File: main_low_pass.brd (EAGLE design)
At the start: 45.4 x 25.6 mm, 16 parts, among them IC1 74HC14D, X1 14867

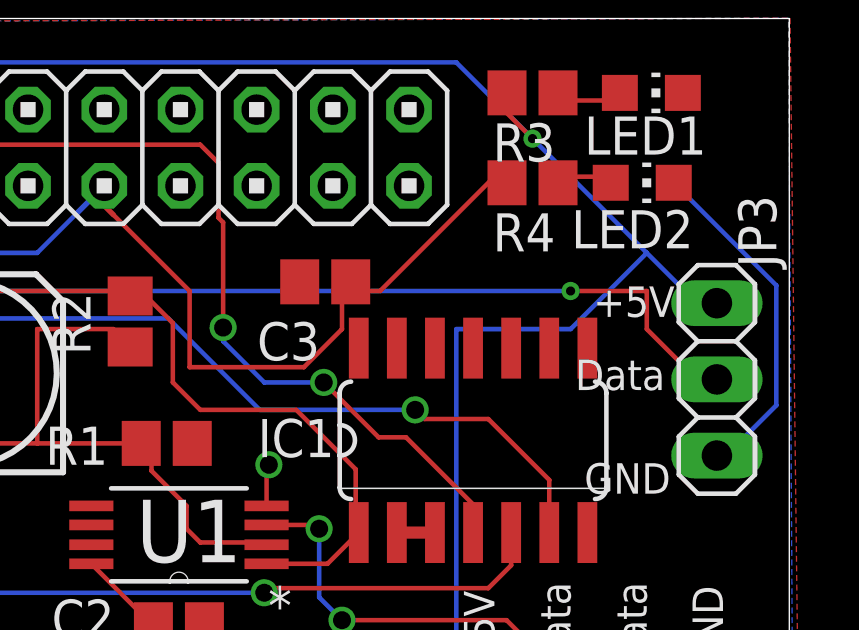
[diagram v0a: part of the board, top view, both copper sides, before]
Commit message: First set of fixes: Missed some connections to IC1
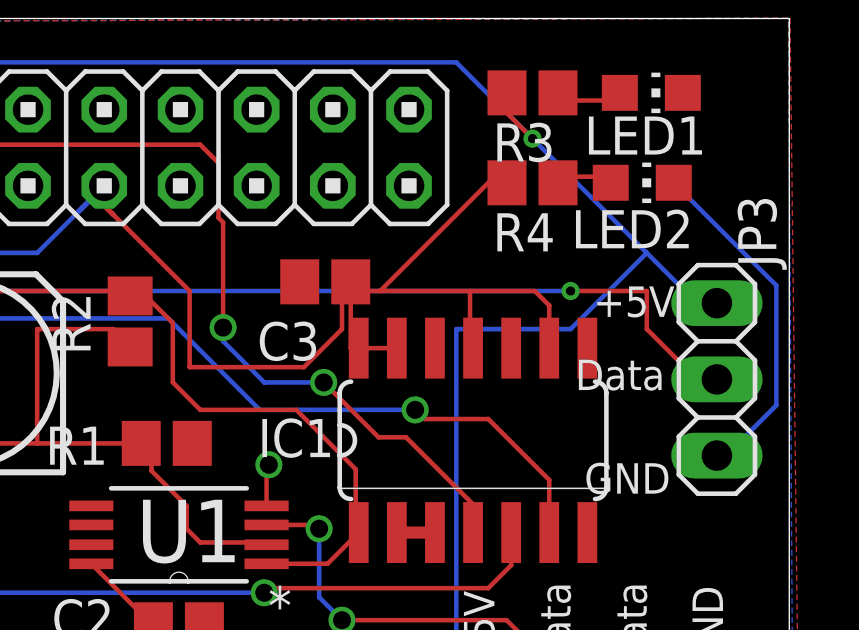
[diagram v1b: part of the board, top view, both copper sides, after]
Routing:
- net VCC: track 44.9 -> 57.9 mm
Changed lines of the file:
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@@
 <wire x1="22.86" y1="17.78" x2="22.5552" y2="18.0848" width="0.1778" layer="1"/>
 <wire x1="22.5552" y1="18.0848" x2="22.5552" y2="18.7452" width="0.1778" layer="1"/>
-<wire x1="34.8488" y1="13.335" x2="37.3888" y2="13.335" width="0" layer="19" extent="1-1"/>
-<wire x1="32.3088" y1="13.335" x2="34.8488" y2="13.335" width="0" layer="19" extent="1-1"/>
-<wire x1="31.0388" y1="13.335" x2="32.3088" y2="13.335" width="0" layer="19" extent="1-1"/>
-<wire x1="30.48" y1="13.97" x2="31.0388" y2="13.335" width="0" layer="19" extent="1-1"/>
+<wire x1="30.7712" y1="13.335" x2="30.7712" y2="15.5448" width="0.1524" layer="1"/>
+<wire x1="37.3888" y1="13.335" x2="37.3888" y2="14.7574" width="0.1524" layer="1"/>
+<wire x1="37.3888" y1="14.7574" x2="36.9062" y2="15.24" width="0.1524" layer="1"/>
+<wire x1="36.9062" y1="15.24" x2="34.7472" y2="15.24" width="0.1524" layer="1"/>
+<wire x1="34.7472" y1="15.24" x2="31.75" y2="15.24" width="0.1524" layer="1"/>
+<wire x1="34.8488" y1="13.335" x2="34.7472" y2="13.4366" width="0.1524" layer="1"/>
+<wire x1="34.7472" y1="13.4366" x2="34.7472" y2="15.24" width="0.1524" layer="1"/>
+<wire x1="32.3088" y1="13.335" x2="31.0388" y2="13.335" width="0.1524" layer="1"/>
+<wire x1="30.7712" y1="13.335" x2="31.0388" y2="13.335" width="0.1524" layer="1"/>
 </signal>
 <signal name="N$3">

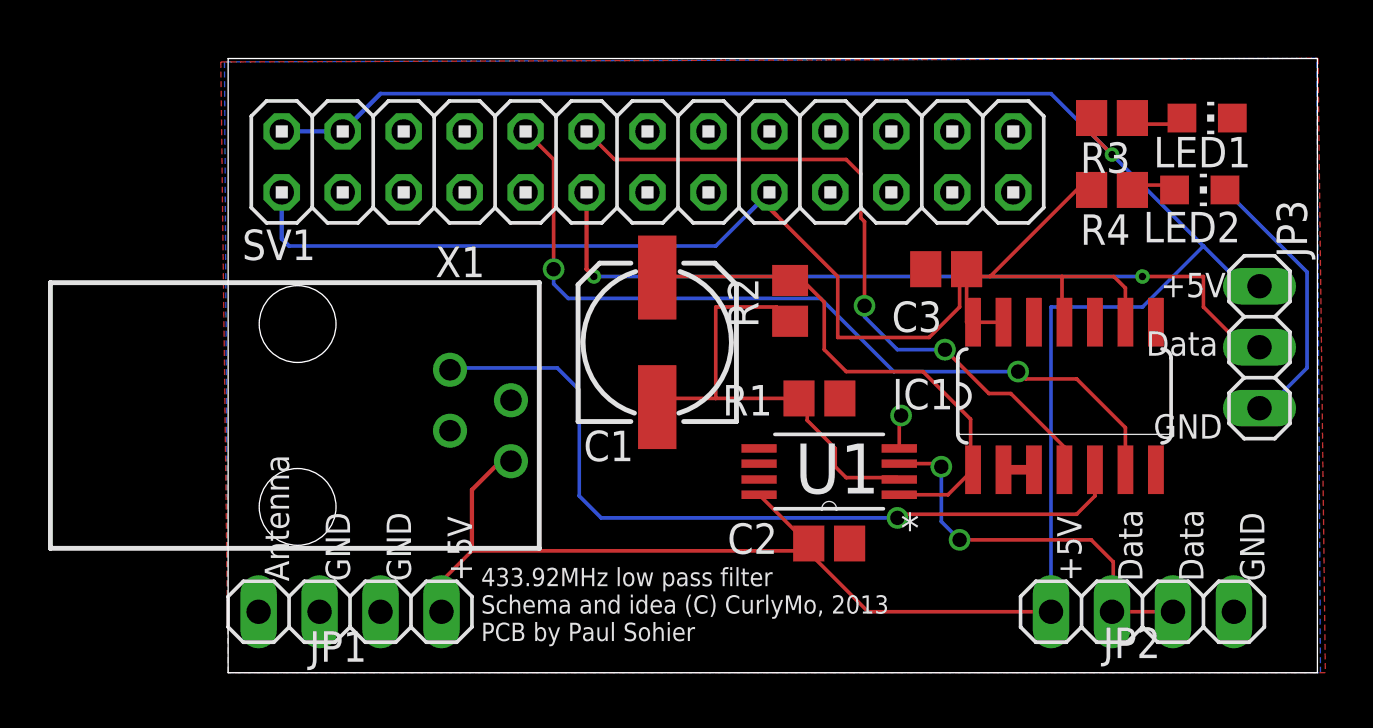
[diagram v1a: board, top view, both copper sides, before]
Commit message: Make sure the low pass filter actually fits the pi. this change causes the board to be outside the pi, but otherwise it hits the analog out.
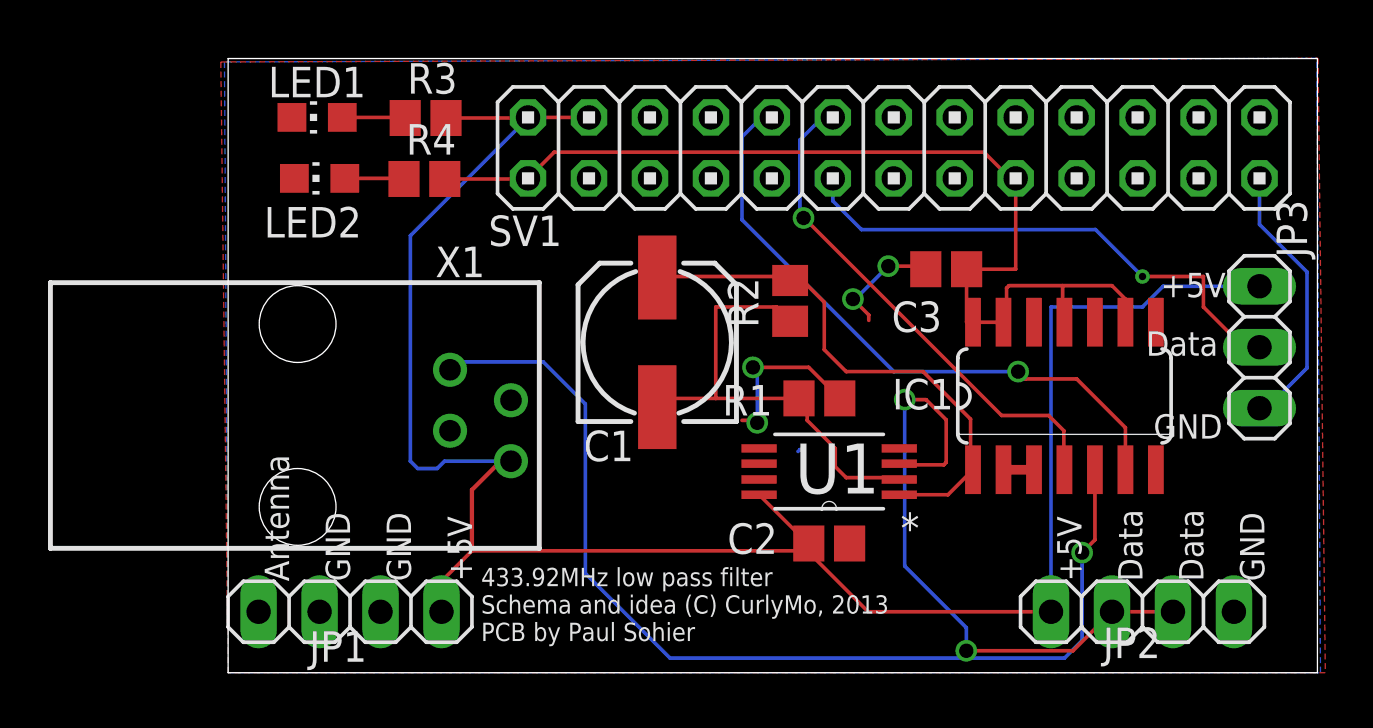
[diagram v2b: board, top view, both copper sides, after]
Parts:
- moved LED1 37.1 mm to (3.71, 21.9), turned to 90 degrees
- moved LED2 36.7 mm to (3.81, 19.3), turned to 90 degrees
- moved R4 28.7 mm to (8.18, 19.3), turned to 0 degrees
- moved R3 28.6 mm to (8.23, 21.8), turned to 0 degrees
- moved SV1 10.3 mm to (27.7, 20.6)
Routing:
- net N$6: track 103.1 -> 84.6 mm
- net VCC: track 57.9 -> 43.5 mm
- net N$5: track 33.2 -> 22.0 mm, vias 2 -> 1
- net GND: track 13.3 -> 23.7 mm, vias 1 -> 4
- net N$1: track 16.6 -> 26.8 mm
- net N$4: track 33.6 -> 43.3 mm
- net N$11: track 34.9 -> 26.4 mm, vias 2 -> 1
- net N$10: track 29.7 -> 21.2 mm, vias 2 -> 1
- net N$9: track 1.95 -> 2.49 mm
